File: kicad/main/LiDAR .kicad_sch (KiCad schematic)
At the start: 7 parts, among them Q20 AO3400, U3 HC-PM254-5_0H-2X4PS-02A

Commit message: Cliff/bumpers connector
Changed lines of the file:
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@@
 	(generator_version "10.0")
 	(paper "A2")
+	(rectangle
+		(start 260.35 182.88)
+		(end 274.32 199.39)
+		(stroke
+			(width 0)
+			(type solid)
+		)
+		(fill
+			(type color)
+			(color 132 0 0 1)
+		)
+	)
+	(rectangle
+		(start 245.11 194.31)
+		(end 257.81 199.39)
+		(stroke
+			(width 0)
+			(type solid)
+		)
+		(fill
+			(type color)
+			(color 132 0 0 1)
+		)
+	)
+	(rectangle
+		(start 219.71 161.29)
+		(end 382.27 233.68)
+		(stroke
+			(width 0)
+			(type solid)
+		)
+		(fill
+			(type color)
+			(color 0 72 0 1)
+		)
+	)
 	(text "LiDAR"
 		(exclude_from_sim no)

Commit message: Second review round
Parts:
- removed C139: 10uF/25V, Capacitor_SMD:C_0603_1608Metric, symbol JLCImport:CL21A106KBYQNNE
- removed D10: SS34, Diode_SMD:D_SMA, symbol DesignLibrary:LiDAR_1_DIODE-2_DesignLibrary.SchLib
- removed Q20: AO3400, oomwoo_altium:SOT23-3D, symbol DesignLibrary:LiDAR_0_N-MOS-SOT23_DesignLibrary.SchLib
- removed R118: 100k, Resistor_SMD:R_0603_1608Metric, symbol DesignLibrary:LiDAR_1_Resistor-1_DesignLibrary.SchLib
- removed R65: 1k, Resistor_SMD:R_0603_1608Metric, symbol Device:R_US
- removed U3: HC-PM254-5_0H-2X4PS-02A, JLCImport:HC-PM254-5_0H-2X4PS-02A, symbol JLCImport:HC-PM254-5_0H-2X4PS-02A
- added C152, C153: 10uF/25V, Capacitor_SMD:C_0603_1608Metric, symbol JLCImport:CL21A106KBYQNNE
- added LIDAR1: WAFER-GH1_25-4PWB, JLCImport:WAFER-GH1_25-4PWB, symbol JLCImport:WAFER-GH1_25-4PWB
- added LIDAR2: HX_PM2_54-1X4P_WT, JLCImport:HX_PM2_54-1X4P_WT, symbol JLCImport:HX_PM2_54-1X4P_WT
- added R66: 1k, Resistor_SMD:R_0603_1608Metric, symbol Device:R_US
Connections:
- net GND: now also C152.2, C153.2, LIDAR1.2, LIDAR1.5, LIDAR1.6, LIDAR2.3
- net LiDAR-MOTOR-CTRL: now also LIDAR1.1
- net LiDAR-RXD: now also R66.1
- net LiDAR-TXD: now also LIDAR1.3
- net VCC-5V-REG: now also C152.1, C153.1, LIDAR1.4, LIDAR2.4
- new net: LIDAR2.1, R66.2
- new net LiDAR-EN: LIDAR2.2
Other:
- moved on the sheet: R116

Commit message: STM32 power rail switch
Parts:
- added D11: SS34, Diode_SMD:D_SMA, symbol DesignLibrary:LiDAR_1_DIODE-2_DesignLibrary.SchLib
- added Q20: AO3400, oomwoo_altium:SOT23-3D, symbol DesignLibrary:LiDAR_0_N-MOS-SOT23_DesignLibrary.SchLib
- C152, C153: value 10uF/25V -> 10uF/10V; LCSC C96446 -> C19702
- R116: LCSC (none) -> C2907088; VOLTAGERATE * -> (none)
- R66: LCSC (none) -> C2907113
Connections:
- net GND: now also D11.1 (A), Q20.2 (S), Q20.3 (D)
- net LiDAR-MOTOR-CTRL: now also Q20.1 (G)
- net VCC-5V-REG: now also D11.2 (K)

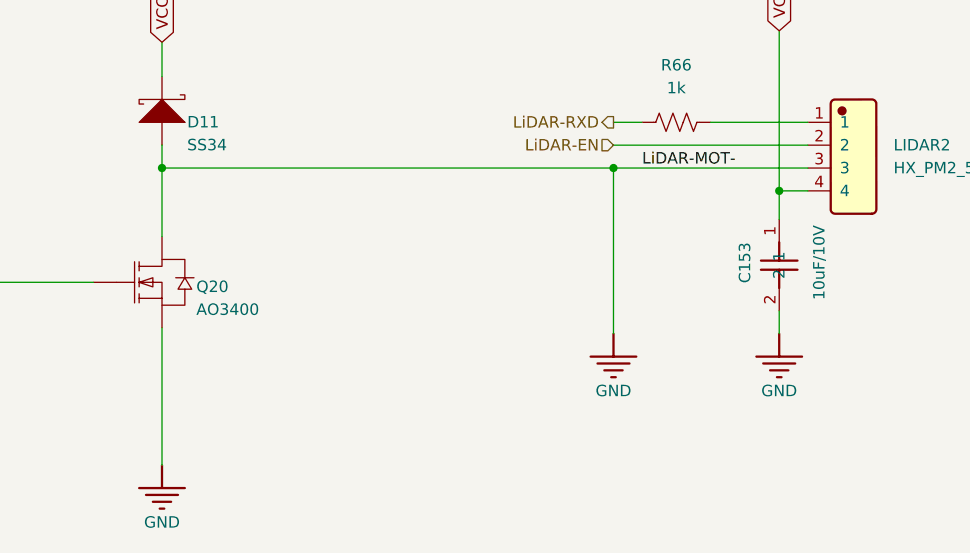
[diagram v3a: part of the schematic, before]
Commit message: Fix Q20 gate GND short
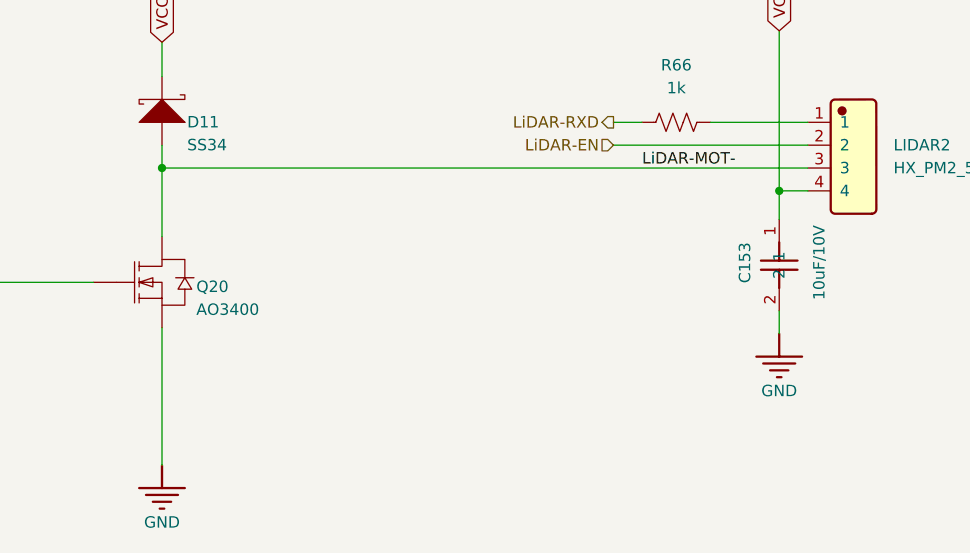
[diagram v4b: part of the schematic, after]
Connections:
- net GND: no longer D11.1 (A), LIDAR2.3, Q20.3 (D)
- new net LiDAR-MOT-: D11.1 (A), LIDAR2.3, Q20.3 (D)
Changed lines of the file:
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@@
-	)
-	(junction
-		(at 274.32 251.46)
-		(diameter 0)
-		(color 0 0 0 0)
 	)
 	(junction
@@
 	(wire
 		(pts
-			(xy 224.155 251.46) (xy 274.32 251.46)
+			(xy 224.155 251.46) (xy 295.91 251.46)
 		)
 		(stroke
@@
 	(wire
 		(pts
-			(xy 274.32 251.46) (xy 274.32 269.875)
-		)
-		(stroke
-			(width 0)
-			(type default)
-		)
-	)
-	(wire
-		(pts
 			(xy 282.575 192.405) (xy 253.365 192.405)
 		)
@@
 		(pts
 			(xy 274.32 246.38) (xy 277.495 246.38)
-		)
-		(stroke
-			(width 0)
-			(type default)
-		)
-	)
-	(wire
-		(pts
-			(xy 274.32 251.46) (xy 295.91 251.46)
 		)
 		(stroke
@@
 					(unit 1)
 				)
-			)
-		)
-	)
-	(symbol
-		(lib_id "oomwoo-kicad-altium-import:GND_POWER_GROUND")
-		(at 274.32 269.875 0)
-		(unit 1)
-		(body_style 1)
-		(exclude_from_sim no)
-		(in_bom yes)
-		(on_board yes)
-		(in_pos_files yes)
-		(dnp no)
-		(property "Reference" "#PWR0653"
-			(at 274.32 269.875 0)
-			(hide yes)
-			(show_name no)
-			(do_not_autoplace no)
-			(effects
-				(font
-					(size 1.27 1.27)
-				)
-			)
-		)
-		(property "Value" "GND"
-			(at 274.32 276.225 0)
-			(show_name no)
-			(do_not_autoplace no)
-			(effects
-				(font
-					(size 1.27 1.27)
-				)
-			)
-		)
-		(property "Footprint" ""
-			(at 274.32 269.875 0)
-			(show_name no)
-			(do_not_autoplace no)
-			(effects
-				(font
-					(size 1.27 1.27)
-				)
-			)
-		)
-		(property "Datasheet" ""
-			(at 274.32 269.875 0)
-			(show_name no)
-			(do_not_autoplace no)
-			(effects
-				(font
-					(size 1.27 1.27)
-				)
-			)
-		)
-		(property "Description" ""
-			(at 274.32 269.875 0)
-			(show_name no)
-			(do_not_autoplace no)
-			(effects
-				(font
-					(size 1.27 1.27)
-				)
-			)
-		)
-		(pin ""
-		)
-		(instances
-			(project "Main"
-				(path "/dbcfb655-8d45-4808-9a74-2a0eb03372e8/994d55da-8e8c-4fe8-9877-f2e4533982e7"
-					(reference "#PWR0653")
-					(unit 1)
-				)
